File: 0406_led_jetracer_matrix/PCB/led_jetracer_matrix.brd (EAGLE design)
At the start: 31.8 x 31.8 mm, 37 parts

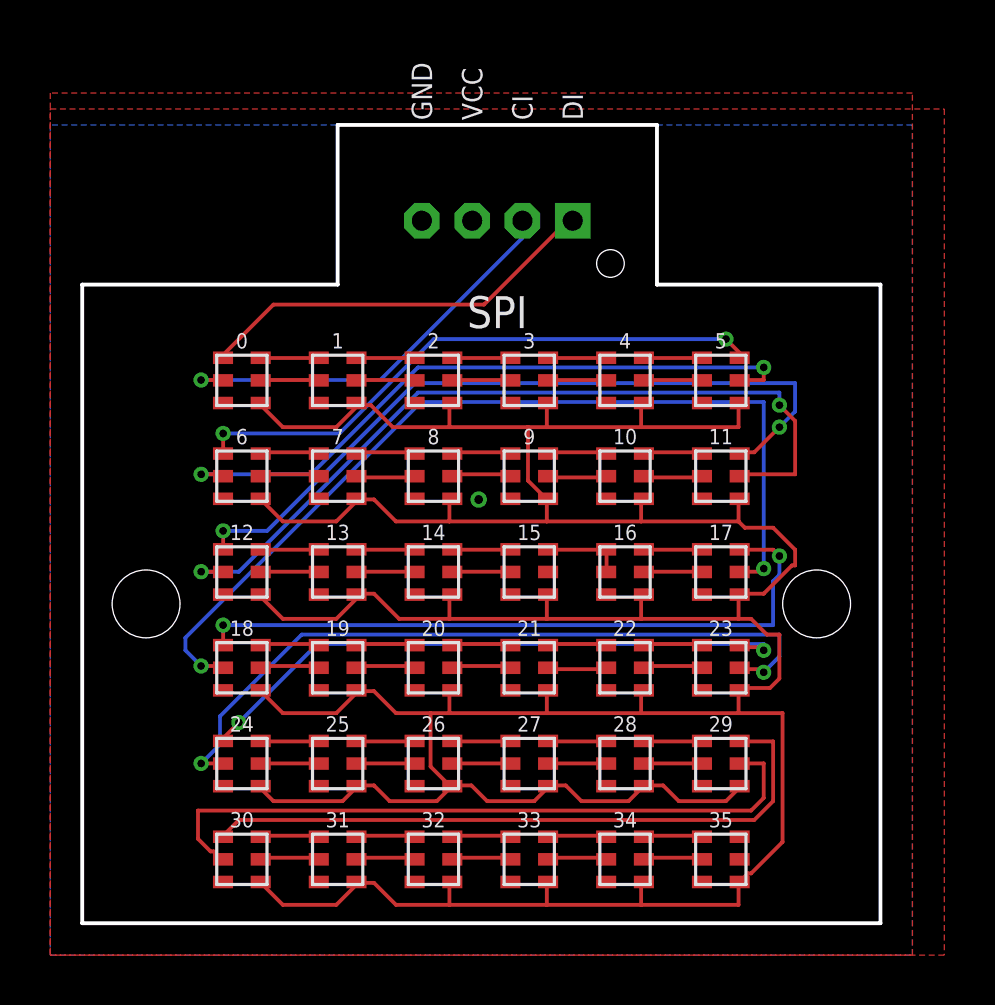
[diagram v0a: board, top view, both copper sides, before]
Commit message: #406 led_jetracer_matrix　ロゴ修正
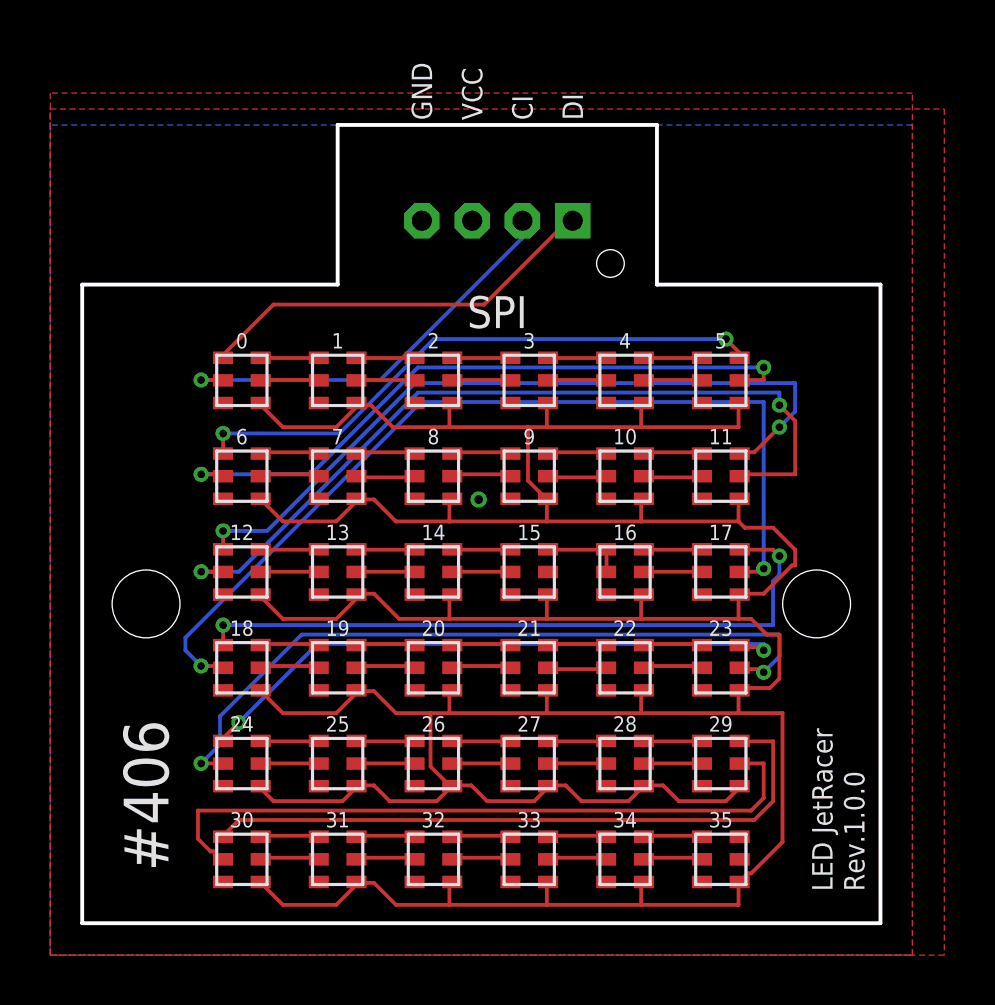
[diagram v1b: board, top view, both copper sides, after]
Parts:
- added LOGO1: (no value), component:LOGO_FABO_M_BOTTOM
- added U$3: LOGO_OSHW-S_BOTTOM, component:LOGO_OSHW_S_BOTTOM
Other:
- board text added: "#406"
- board text added: "Designed in Aizu"
- board text added: "LED JetRacer"
- board text added: "Rev.1.0.0"
